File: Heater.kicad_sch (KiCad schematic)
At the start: 87 parts, among them J1 Conn_01x02_Socket, J2 Conn_01x02_Socket, J3 Debug, J4 OLED, J5 Conn_01x02_Pin, Q1 NMOS, Q2 NMOS, SW1 RotaryEncoder_Switch, SW2 SW_MEC_5E, SW3 SW_MEC_5E, SW4 SW_MEC_5E, SW5 SW_MEC_5E, U1 STM32H750VBTx, U3 W25Q128JVS, U4 AD8495, U5 AD8495, U6 TLV62569DBV, Y1 32768Hz, Y2 25MHz

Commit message: feat: 完成弱电部分的原理图绘制
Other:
- company: (none) -> MaQjianJin
- title: (none) -> Low Voltage Part
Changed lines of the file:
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@@
 	(generator_version "9.0")
 	(paper "A4")
+	(title_block
+		(title "Low Voltage Part")
+		(date "2025-05-27")
+		(rev "0.1")
+		(company "MaQjianJin")
+	)
 	(text "OLED"
 		(exclude_from_sim no)

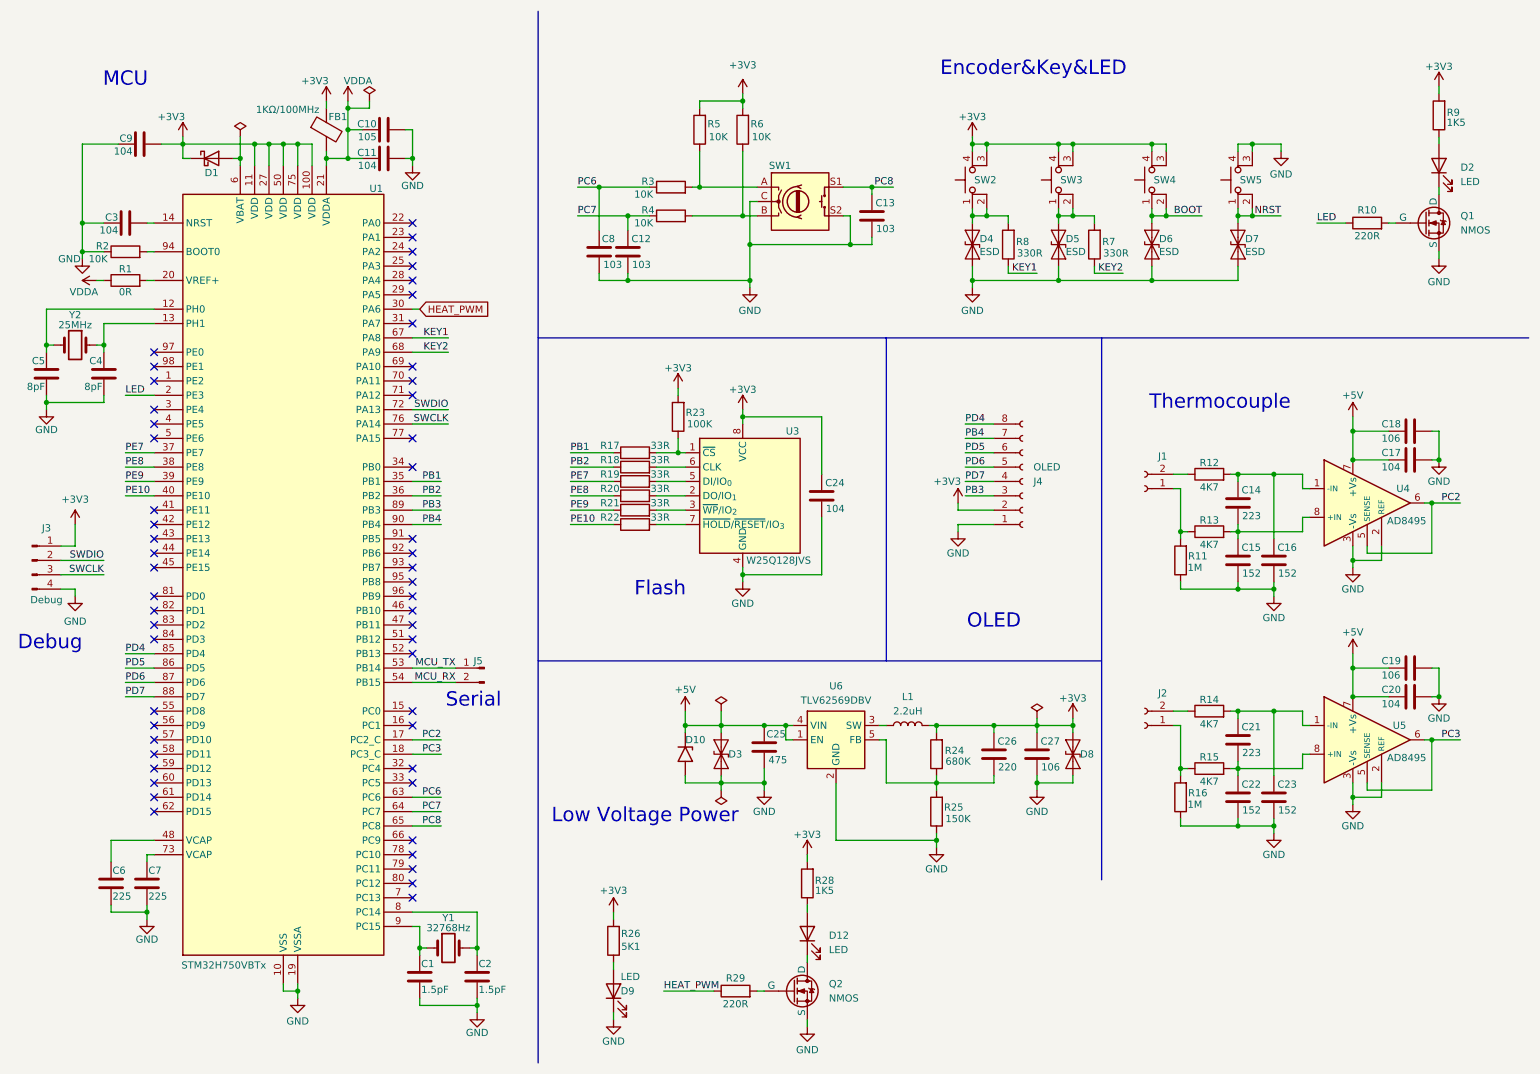
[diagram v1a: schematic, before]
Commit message: fix: 调整了全部元件的位号，并重新设计了加热端的驱动部分
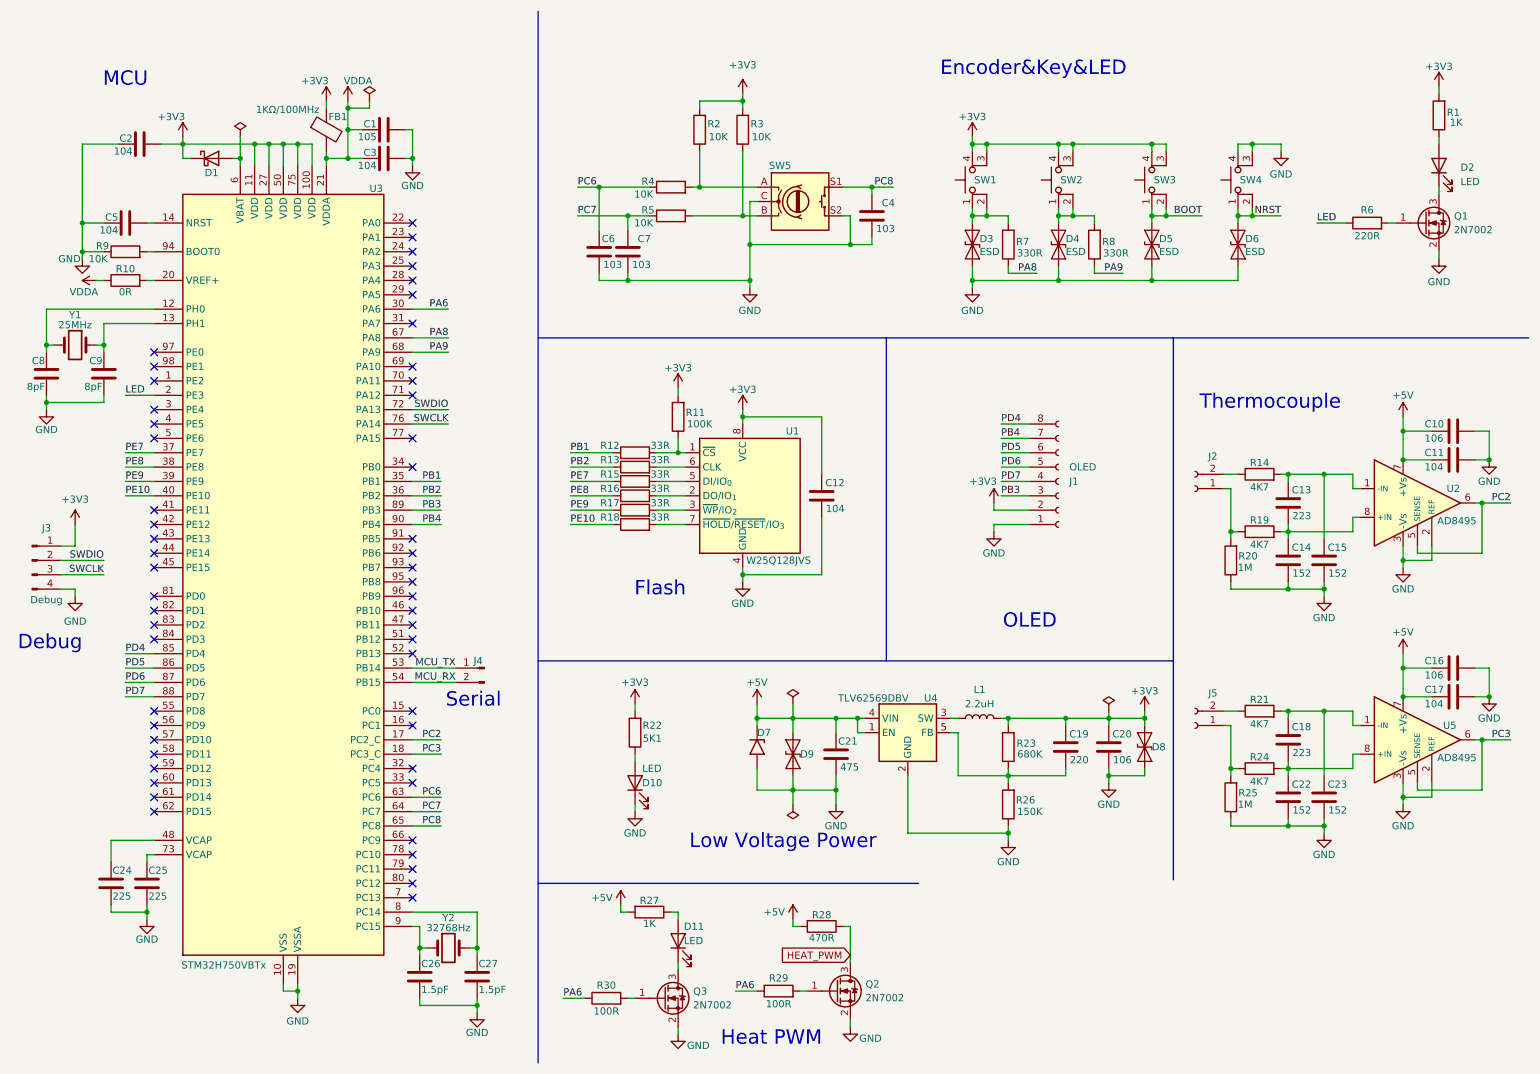
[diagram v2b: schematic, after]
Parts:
- removed Q1, Q2: NMOS, symbol Simulation_SPICE:NMOS
- added Q1, Q2, Q3: 2N7002, Package_TO_SOT_SMD:SOT-23, symbol Transistor_FET:2N7002
- added R28: 470R, symbol Device:R
- added R29: 100R, symbol Device:R
- R1: renamed from R9; value 1K5 -> 1K
- R27: renamed from R28; value 1K5 -> 1K
- R30: renamed from R29; value 220R -> 100R
- renumbered C10 to C1, C18 to C10, C17 to C11, C24 to C12, C14 to C13, C15 to C14, C16 to C15, C19 to C16, C20 to C17, C21 to C18, C26 to C19, C9 to C2, C27 to C20, C25 to C21, C6 to C24, C7 to C25, C1 to C26, C2 to C27, C11 to C3, C13 to C4, C3 to C5, C8 to C6, C12 to C7, C5 to C8, C4 to C9, D9 to D10, D12 to D11, D4 to D3, D5 to D4, D6 to D5, D7 to D6, D10 to D7, D3 to D9, J4 to J1, J1 to J2, J5 to J4, J2 to J5, R1 to R10, R23 to R11, R17 to R12, R18 to R13, R12 to R14, R19 to R15, R20 to R16, R21 to R17, R22 to R18, R13 to R19, R5 to R2, R11 to R20, R14 to R21, R26 to R22, R24 to R23, R15 to R24, R16 to R25, R25 to R26, R6 to R3, R3 to R4, R4 to R5, R10 to R6, R8 to R7, R7 to R8, R2 to R9, SW2 to SW1, SW3 to SW2, SW4 to SW3, SW5 to SW4, SW1 to SW5, U3 to U1, U4 to U2, U1 to U3, U6 to U4, Y2 to Y1, Y1 to Y2
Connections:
- net +3V3: no longer R27.2
- net +5V: now also R27.2, R28.2
- net GND: now also Q1.2 (S), Q2.2 (S), Q3.2 (S)
- net HEAT_PWM: now also Q2.3 (D), R28.1; no longer R30.1, U3.30 (PA6)
- net at D11.1 (K): now also Q3.3 (D)
- net at R30.2: now also Q3.1 (G)
- net at D2.1 (K): now also Q1.3 (D)
- net at R6.2: now also Q1.1 (G)
- net KEY1 renamed PA8
- net KEY2 renamed PA9
- new net: Q2.1 (G), R29.2
- new net PA6: R29.1, R30.1, U3.30 (PA6)
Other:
- note added: "Heat PWM"
- moved on the sheet: C10, C11, C13, C14, C15, C16, C17, C18, C19, C20, C21, C22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

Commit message: feat: 完成元件选型和封装设置
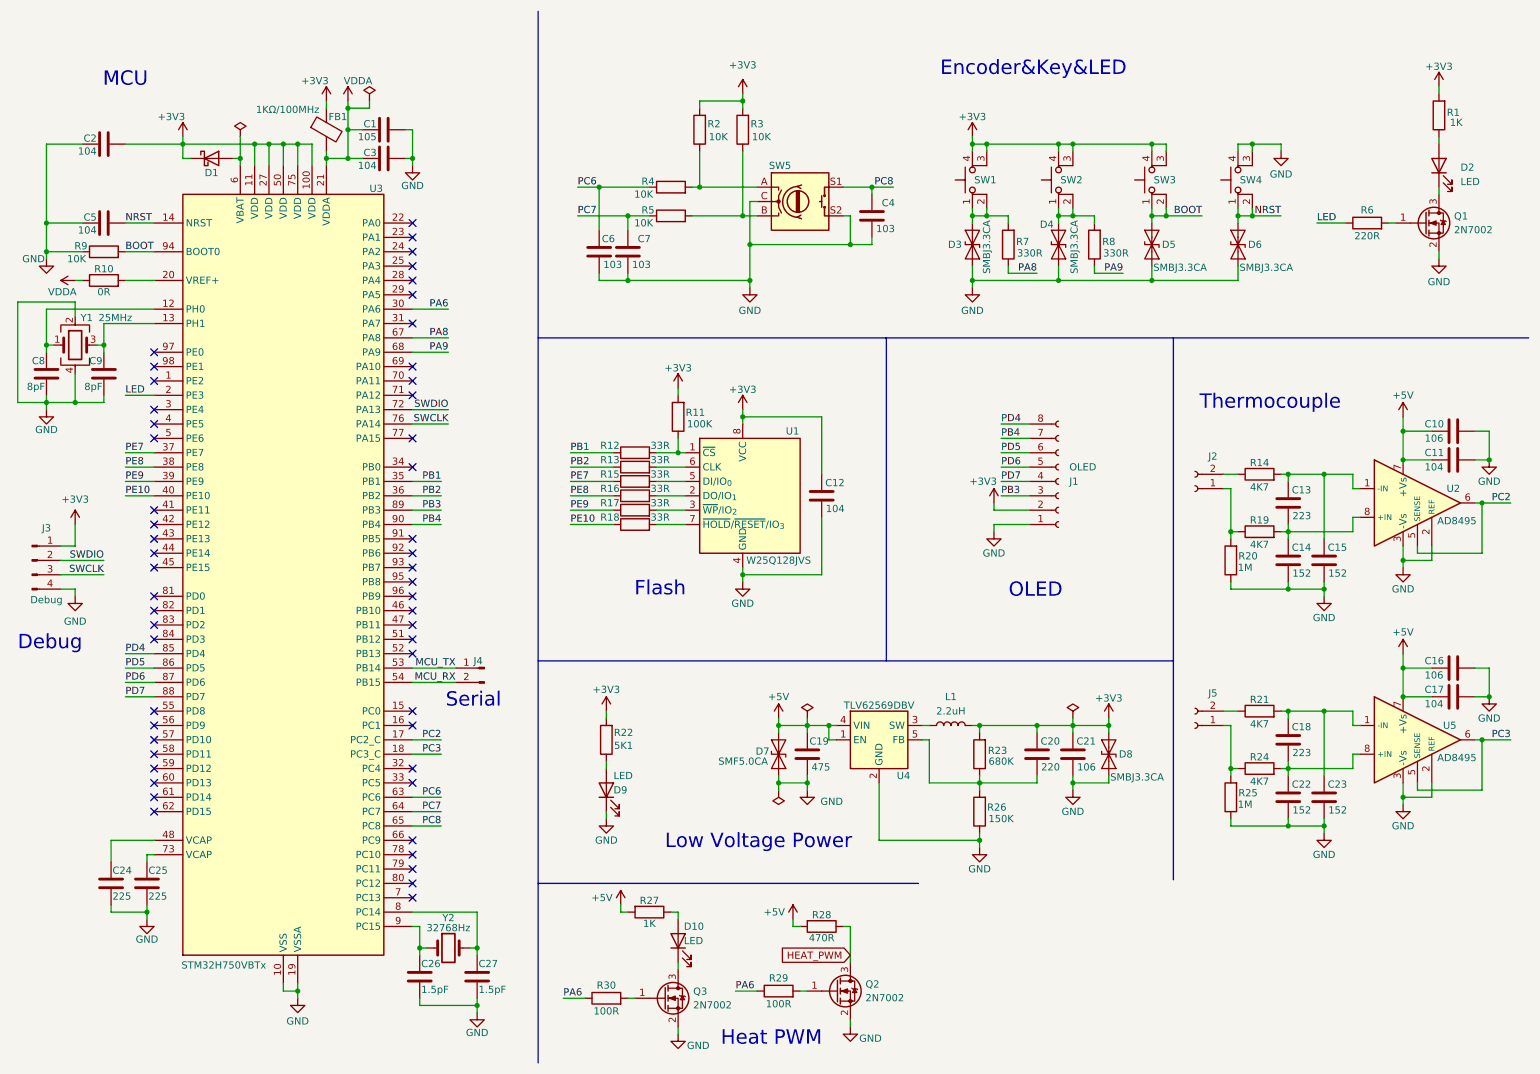
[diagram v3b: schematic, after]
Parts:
- removed D7: SM6T6V8A, Diode_SMD:D_SMB, symbol Diode:SM6T6V8A
- removed D9: SZESD9B5.0ST5G, Diode_SMD:D_SOD-923, symbol Diode:SZESD9B5.0ST5G
- removed Y1: 25MHz, symbol Device:Crystal
- added D7: SMF5.0CA, Diode_SMD:D_SOD-123F, symbol Diode:ESD9B3.3ST5G
- added Y1: 25MHz, Crystal:Crystal_SMD_3225-4Pin_3.2x2.5mm_HandSoldering, symbol Device:Crystal_GND24
- C1, C10, C11, C12, C13, C14, C15, C16, C17, C18, C2, C22, C23, C24, C25, C26, C27, C3, C4, C5, C6, C7, C8, C9, FB1: footprint (none) -> Capacitor_SMD:C_0603_1608Metric_Pad1.08x0.95mm_HandSolder
- C19: renamed from C21; footprint (none) -> Capacitor_SMD:C_0603_1608Metric_Pad1.08x0.95mm_HandSolder
- C20: renamed from C19; footprint (none) -> Capacitor_SMD:C_0603_1608Metric_Pad1.08x0.95mm_HandSolder
- C21: renamed from C20; footprint (none) -> Capacitor_SMD:C_0603_1608Metric_Pad1.08x0.95mm_HandSolder
- D1: footprint (none) -> Diode_SMD:D_SOD-123
- D10: renamed from D11; footprint (none) -> Diode_SMD:D_0603_1608Metric_Pad1.05x0.95mm_HandSolder
- D2: footprint (none) -> Diode_SMD:D_0603_1608Metric_Pad1.05x0.95mm_HandSolder
- D3, D4, D5, D6: value ESD -> SMBJ3.3CA; footprint Diode_SMD:D_SOD-923 -> Diode_SMD:D_SMB_Handsoldering
- D8: value SZESD9B5.0ST5G -> SMBJ3.3CA; footprint Diode_SMD:D_SOD-923 -> Diode_SMD:D_SMB_Handsoldering
- D9: renamed from D10; footprint (none) -> Diode_SMD:D_0603_1608Metric_Pad1.05x0.95mm_HandSolder
- J1: footprint (none) -> Connector_PinHeader_2.54mm:PinHeader_1x08_P2.54mm_Vertical
- J2, J4, J5: footprint (none) -> Connector_PinHeader_2.54mm:PinHeader_1x02_P2.54mm_Vertical
- J3: footprint (none) -> Connector_PinHeader_2.54mm:PinHeader_1x04_P2.54mm_Vertical
- L1: footprint (none) -> Inductor_SMD:L_0603_1608Metric_Pad1.05x0.95mm_HandSolder
- Q1, Q2, Q3: footprint Package_TO_SOT_SMD:SOT-23 -> Package_TO_SOT_SMD:SOT-23_Handsoldering
- R1, R10, R11, R12, R13, R14, R15, R16, R17, R18, R19, R2, R20, R21, R22, R23, R24, R25, R26, R27, R28, R29, R3, R30, R4, R5, R6, R7, R8, R9: footprint (none) -> Resistor_SMD:R_0603_1608Metric_Pad0.98x0.95mm_HandSolder
- SW1, SW2, SW3, SW4: footprint (none) -> HeaterLibrary:SW_Buttom_SMD_5.1mmx5.1mm
- SW5: footprint (none) -> HeaterLibrary:RotaryEncoder_Switch_EC11_SMD
- Y2: footprint (none) -> Crystal:Crystal_SMD_3215-2Pin_3.2x1.5mm
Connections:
- net +5V: now also D7.2 (A2)
- net BOOT: now also D5.1 (A1), R9.2, U3.94 (BOOT0); no longer D5.2 (A2)
- net GND: now also D3.2 (A2), D4.2 (A2), D5.2 (A2), D6.2 (A2), D7.1 (A1), Y1.2, Y1.4; no longer D3.1 (A1), D4.1 (A1), D5.1 (A1), D6.1 (A1)
- net NRST: now also C5.2, D6.1 (A1), U3.14 (NRST); no longer D6.2 (A2)
- net at R7.2, SW1.1, SW1.2: now also D3.1 (A1); no longer D3.2 (A2)
- net at R8.2, SW2.1, SW2.2: now also D4.1 (A1); no longer D4.2 (A2)
- net at C9.1, U3.13 (PH1): now also Y1.3
- net at C8.1, U3.12 (PH0): now also Y1.1
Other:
- moved on the sheet: C19, C2, C20, C21, C5, D8, D9, L1, R10, R22, R23, R26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
